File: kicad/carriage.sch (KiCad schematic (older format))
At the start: 39 parts, among them CON10 Stepstick_Right_Connector, CON11 Stepstick_Left_Connector, CON12 Stepstick_Right_Connector, CON13 Carriage, CON14 Stepstick_Left_Connector, CON15 Stepstick_Right_Connector, CON9 Stepstick_Left_Connector, Q1 IRLR2905ZPBF, Q2 IRLR2905ZPBF, U1 CD4504BPW, U2 ULN2803ADW

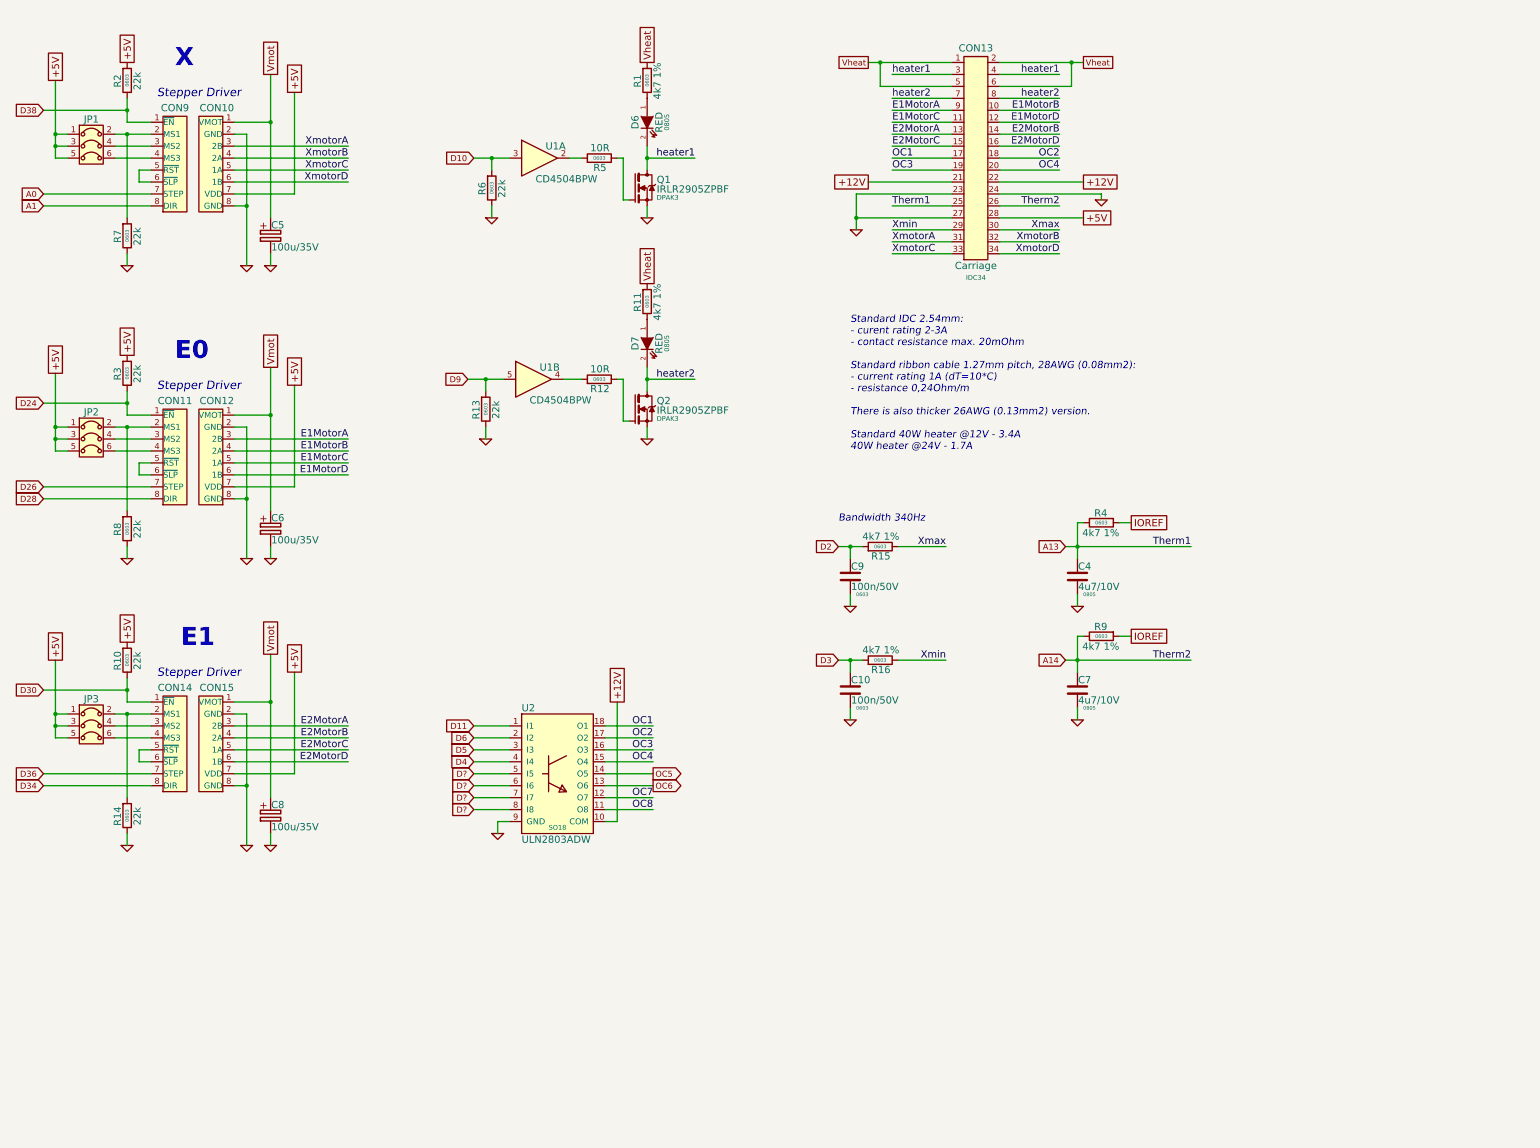
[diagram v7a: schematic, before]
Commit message: Change ULN2803 to discrete MOSFET's FDC6401N
Close #7
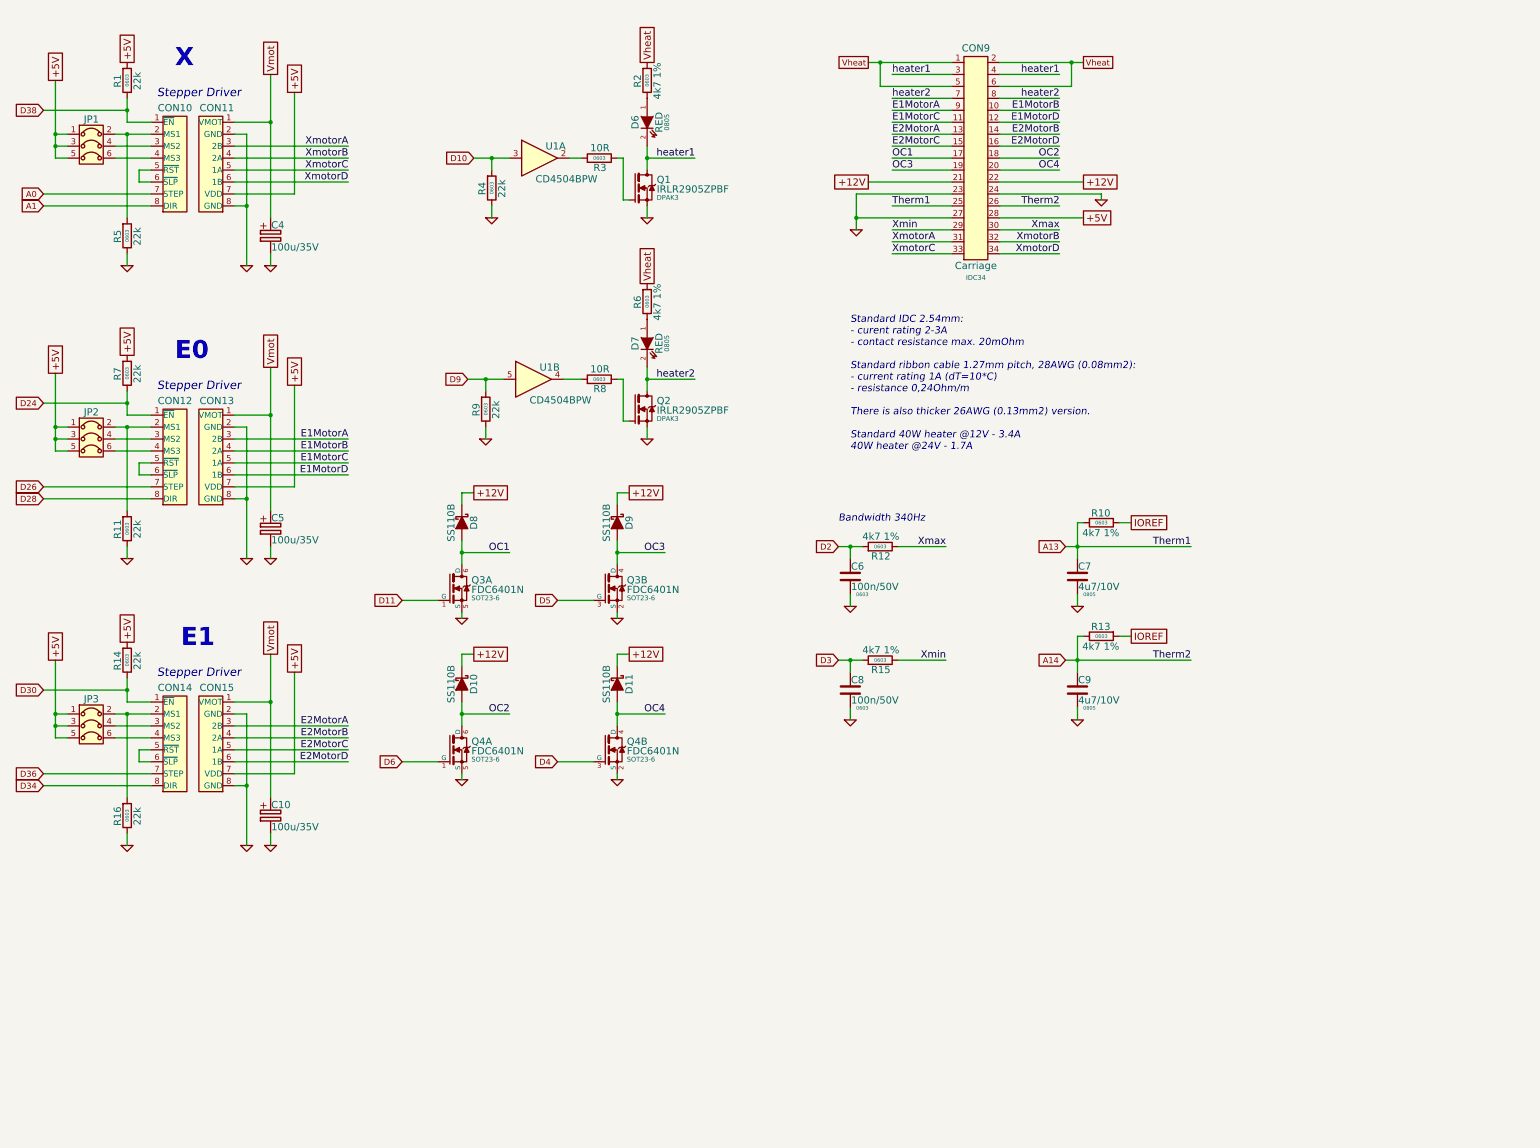
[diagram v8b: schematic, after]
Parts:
- removed U2: ULN2803ADW, SO18, symbol ULN2803ADW
- added D10, D11, D8, D9: SS110B, symbol SS110B
- added Q3, Q4: FDC6401N, SOT23-6, symbol FDC6401N
- renumbered C8 to C10, C5 to C4, C6 to C5, C9 to C6, C4 to C7, C10 to C8, C7 to C9, CON9 to CON10, CON10 to CON11, CON11 to CON12, CON12 to CON13, CON13 to CON9, R2 to R1, R4 to R10, R8 to R11, R15 to R12, R9 to R13, R10 to R14, R16 to R15, R14 to R16, R1 to R2, R5 to R3, R6 to R4, R7 to R5, R11 to R6, R3 to R7, R12 to R8, R13 to R9
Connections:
- net +12V: now also D10.1, D11.1, D8.1, D9.1
- net D11: now also Q3.1 (G)
- net D4: now also Q4.3 (G)
- net D5: now also Q3.3 (G)
- net D6: now also Q4.1 (G)
- net GND: now also Q3.2 (S), Q3.5 (S), Q4.2 (S), Q4.5 (S)
- net OC1: now also D8.2, Q3.6 (D)
- net OC2: now also D10.2, Q4.6 (D)
- net OC3: now also D9.2, Q3.4 (D)
- net OC4: now also D11.2, Q4.4 (D)
